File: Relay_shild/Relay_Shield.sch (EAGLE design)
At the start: 11 parts, among them K1 G2RE, T1 2N2222

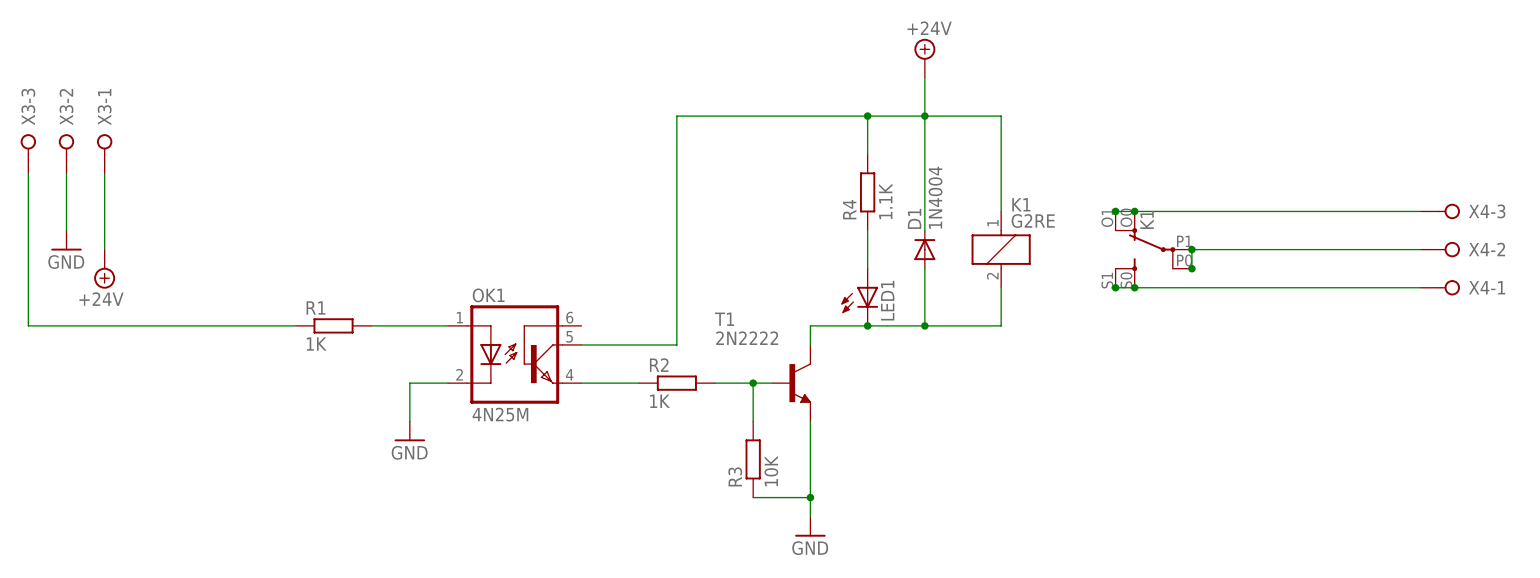
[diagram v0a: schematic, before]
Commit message: added port extender, modified relay shield
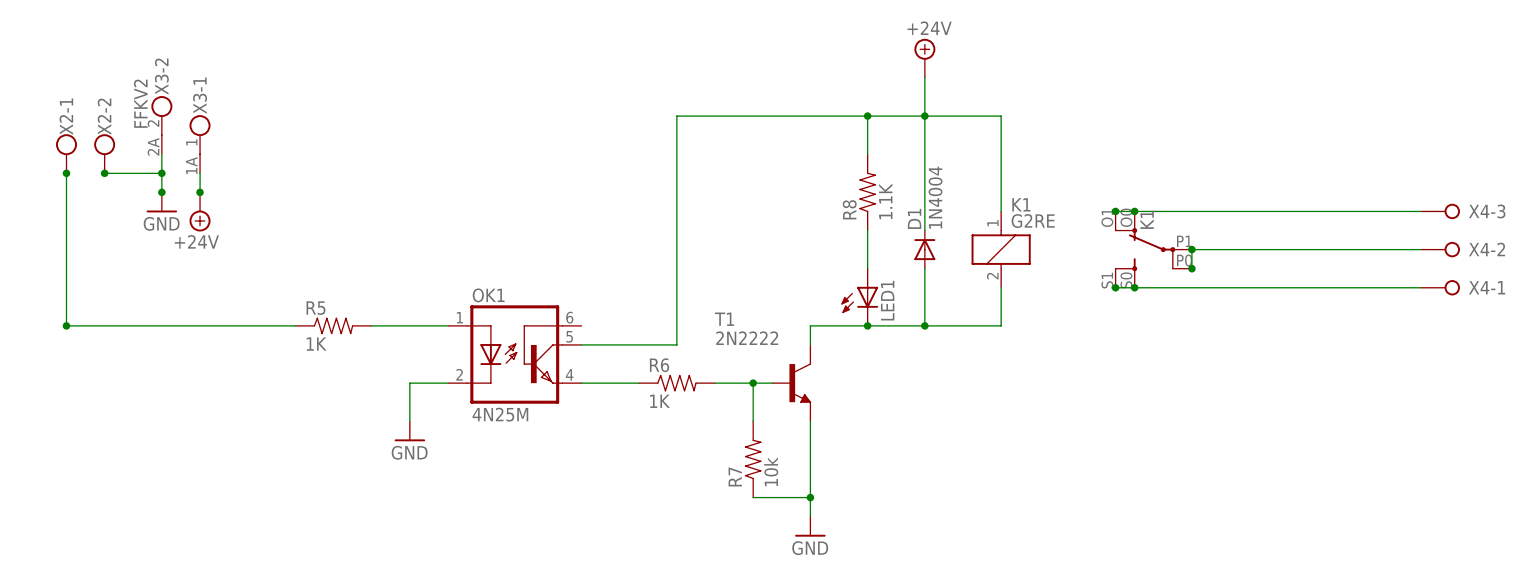
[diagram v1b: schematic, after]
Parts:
- removed R1, R2: 1K, rcl:R-EU_0204/5
- removed R3: 10K, rcl:R-EU_0204/5
- removed R4: 1.1K, rcl:R-EU_0204/5
- added R5, R6: 1K, SparkFun-Passives:RESISTOR1206
- added R7: 10k, SparkFun-Passives:RESISTOR1206
- added R8: 1.1K, SparkFun-Passives:RESISTOR1206
- added X2: (no value), con-wago-500:W237-102
- X3: value (none) -> FFKV2; device con-wago-508:W237-3E -> con-phoenix-508:FFKV2
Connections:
- net +24V: now also R8.2, X3-1.2; no longer R4.2, X3-1.KL
- net GND: now also R7.1, X2-2.KL, X3-2.2; no longer R3.1, X3-2.KL
- net N$1: now also R5.2; no longer R1.2
- net N$2: now also R6.1; no longer R2.1
- net N$3: now also R6.2, R7.2; no longer R2.2, R3.2
- net N$4: now also R5.1, X2-1.KL; no longer R1.1, X3-3.KL
- net N$6: now also R8.1; no longer R4.1
